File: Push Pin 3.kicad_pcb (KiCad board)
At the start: 2 copper layers, 95 x 77.4 mm, 27 parts, among them J1 Screw_Terminal_01x02, J10 Screw_Terminal_01x02, J11 Screw_Terminal_01x02, J12 Screw_Terminal_01x02, J13 Screw_Terminal_01x02, J4 Screw_Terminal_01x02, J5 Screw_Terminal_01x02, J6 Screw_Terminal_01x02, J7 Screw_Terminal_01x02, J8 Screw_Terminal_01x02, J9 Screw_Terminal_01x02, SW1 SW_DPDT_x2, SW2 SW_DPDT_x2, SW3 SW_DPDT_x2, U1 LM2596S-ADJ

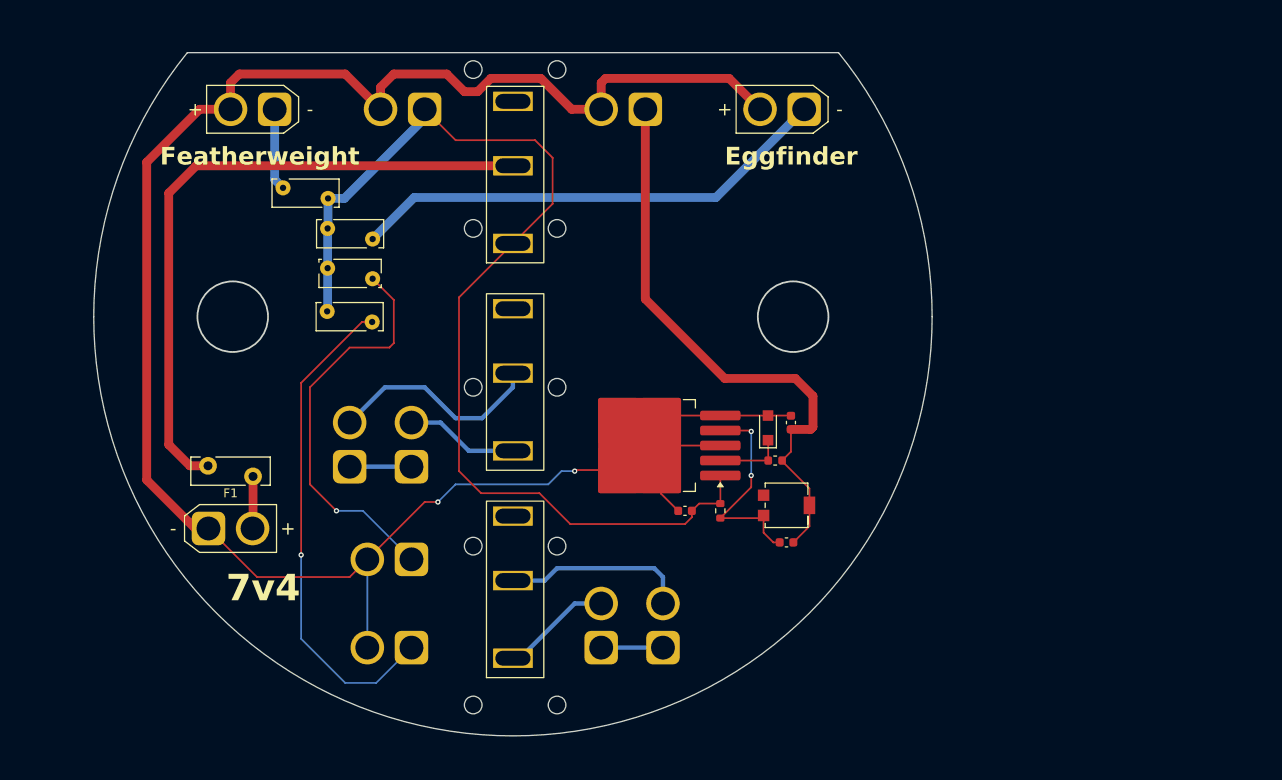
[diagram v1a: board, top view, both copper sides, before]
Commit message: Modif circuits
Ajout des circuits de protection de polarité inverse
Commentaires capacités de découplage
Jumper pour joindre batteries
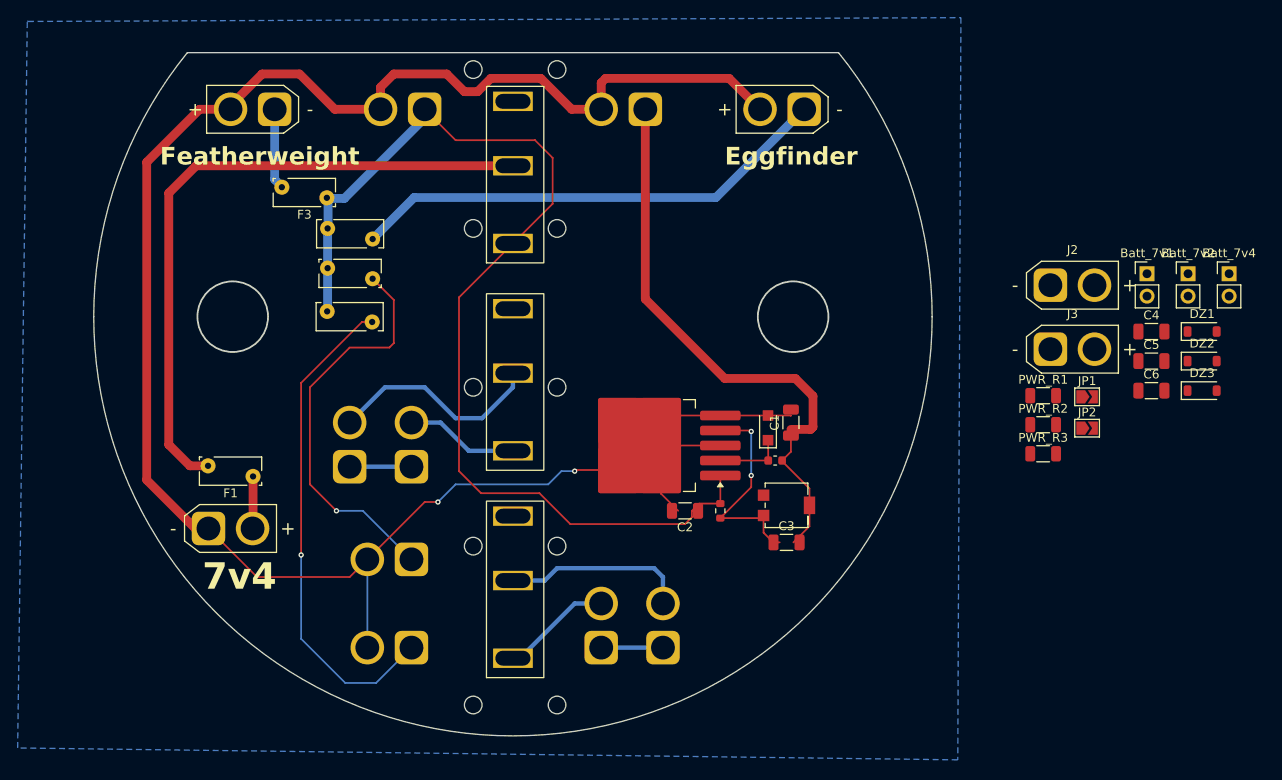
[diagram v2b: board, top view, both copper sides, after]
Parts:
- added Batt_7v1: Batt2_9V, Connector_PinHeader_2.54mm:PinHeader_1x02_P2.54mm_Vertical, F.Cu at (221.8, 95.1)
- added Batt_7v2: Batt1_9V, Connector_PinHeader_2.54mm:PinHeader_1x02_P2.54mm_Vertical, F.Cu at (226.5, 95.1)
- added Batt_7v4: Conn_01x02, Connector_PinHeader_2.54mm:PinHeader_1x02_P2.54mm_Vertical, F.Cu at (231.1, 95.1)
- added C4: 1uF, Capacitor_SMD:C_1206_3216Metric, F.Cu at (222.3, 101.7)
- added C5: 1uF, Capacitor_SMD:C_1206_3216Metric, F.Cu at (222.3, 105.0)
- added C6: 1uF, Capacitor_SMD:C_1206_3216Metric, F.Cu at (222.3, 108.4)
- added DZ1: SZMMSZ4679T1G, Diode_SMD:D_SOD-123, F.Cu at (228.1, 101.7)
- added DZ2: SZMMSZ4679T1G, Diode_SMD:D_SOD-123, F.Cu at (228.1, 105.0)
- added DZ3: SZMMSZ4679T1G, Diode_SMD:D_SOD-123, F.Cu at (228.1, 108.4)
- added J2: Screw_Terminal_01x02, Connector_AMASS:AMASS_XT30U-M_1x02_P5.0mm_Vertical, F.Cu at (210.9, 96.4)
- added J3: Screw_Terminal_01x02, Connector_AMASS:AMASS_XT30U-M_1x02_P5.0mm_Vertical, F.Cu at (210.9, 103.7)
- added JP1: SolderJumper_2_Open, Jumper:SolderJumper-2_P1.3mm_Open_TrianglePad1.0x1.5mm, F.Cu at (215.1, 109.1)
- added JP2: SolderJumper_2_Open, Jumper:SolderJumper-2_P1.3mm_Open_TrianglePad1.0x1.5mm, F.Cu at (215.1, 112.6)
- added PWR_R1: 100k, Resistor_SMD:R_1206_3216Metric, F.Cu at (210.1, 109.0)
- added PWR_R2: 100k, Resistor_SMD:R_1206_3216Metric, F.Cu at (210.1, 112.2)
- added PWR_R3: 100k, Resistor_SMD:R_1206_3216Metric, F.Cu at (210.1, 115.5)
- C1: value 220uF -> 1uF; footprint Capacitor_SMD:C_0603_1608Metric -> Capacitor_SMD:C_1206_3216Metric
- C2: value 150uF -> 1uF; footprint Capacitor_SMD:C_0603_1608Metric -> Capacitor_SMD:C_1206_3216Metric
- C3: value 30pF -> 1uF; footprint Capacitor_SMD:C_0603_1608Metric -> Capacitor_SMD:C_1206_3216Metric
- F1: footprint Fuse:Fuse_Bourns_MF-RHT300 -> Fuse:Fuse_Bourns_MF-RHT070
- F3: footprint Fuse:Fuse_Bourns_MF-RHT050 -> Fuse:Fuse_Bourns_MF-RHT070
- moved F3 0.15 mm to (128.9, 86.5)
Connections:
- C1 pad 1: Net-(J12-Pin_1) -> Net-(J5-Pin_2)
- C1 pad 2: V- -> GND
- C2 pad 1: V+ -> 7v4
- C2 pad 2: V- -> GND
- C3 pad 1: Net-(U1-FB) -> 7v4
- C3 pad 2: Net-(J12-Pin_1) -> GND
- F1 pad 1: Net-(J1-Pin_2) -> Net-(DZ1-K)
- F1 pad 2: Net-(SW3A-B) -> 7v4
- F2 pad 1: V+ -> 7v4
- F2 pad 2: Net-(J8-Pin_1) -> Net-(J1-Pin_2)
- F3 pad 1: V+ -> 7v4
- F3 pad 2: Net-(J13-Pin_1) -> Net-(J5-Pin_2)
- J1 pad 1: V- -> GND
- J4 pad 1: Net-(J4-Pin_1) -> GND
- J4 pad 2: Net-(J4-Pin_2) -> 7v4
- J5 pad 1: Net-(J4-Pin_1) -> GND
- J6 pad 1: Net-(J6-Pin_1) -> GND
- J6 pad 2: Net-(J6-Pin_2) -> 7v4
- J7 pad 1: Net-(J6-Pin_1) -> unconnected-(J7-Pin_1-Pad1)
- J7 pad 2: Net-(J7-Pin_2) -> unconnected-(J7-Pin_2-Pad2)
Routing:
- net Net-(J6-Pin_1): track 7.00 -> 0.00 mm
- net Net-(J4-Pin_1): track 7.00 -> 0.00 mm
- net GND: track 0.00 -> 7.00 mm
- net (no net): track 0.00 -> 7.00 mm
- net V-: track 225.3 -> 223.8 mm
- net Net-(J8-Pin_1): vias 1 -> 0
- net Net-(J1-Pin_2): vias 0 -> 1
- added copper zone on B.Cu, net GND

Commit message: PCB au complet
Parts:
- removed D2: D_Schottky, Diode_SMD:Nexperia_CFP3_SOD-123W
- removed F4, F5: Fuse, Fuse:Fuse_Bourns_MF-RHT050
- removed J10, J11, J12, J13, J8, J9: Screw_Terminal_01x02, Connector_AMASS:AMASS_XT30U-M_1x02_P5.0mm_Vertical
- removed L1: 47uH, Inductor_SMD:L_0603_1608Metric
- removed R1: 1k, Resistor_SMD:R_0603_1608Metric
- removed R2: 2k, Potentiometer_SMD:Potentiometer_Bourns_3214G_Horizontal
- removed SW1, SW2, SW3: SW_DPDT_x2, Library:Omrun_SS-01GL13
- removed U1: LM2596S-ADJ, Package_TO_SOT_SMD:TO-263-5_TabPin3
- added Q1: NTR4101PT1G, NTR4101PT1G:SOT-23-3_1P4X3P040_ONS, F.Cu at (141.0, 90.5)
- added Q2: NTR4101PT1G, NTR4101PT1G:SOT-23-3_1P4X3P040_ONS, B.Cu at (165.0, 126.0)
- added Q3: NTR4101PT1G, NTR4101PT1G:SOT-23-3_1P4X3P040_ONS, F.Cu at (136.0, 97.5)
- added SW4: SW_DPDT_x2, Library:Omrun_SS-01GL13, F.Cu at (150.0, 83.4)
- added SW5: SW_DPDT_x2, Library:Omrun_SS-01GL13, F.Cu at (150.0, 129.9)
- added SW6: SW_DPDT_x2, Library:Omrun_SS-01GL13, F.Cu at (150.0, 106.9)
- added U2: LDO_4v2-MIC5209-4.2YS-TR, footprints:SOT-223_S_MCH, F.Cu at (182.0, 86.2)
- Batt_7v1, Batt_7v2: footprint Connector_PinHeader_2.54mm:PinHeader_1x02_P2.54mm_Vertical -> Connector_AMASS:AMASS_XT30U-M_1x02_P5.0mm_Vertical; moved to B.Cu
- Batt_7v4: footprint Connector_PinHeader_2.54mm:PinHeader_1x02_P2.54mm_Vertical -> Connector_AMASS:AMASS_XT30U-M_1x02_P5.0mm_Vertical
- DZ2, J1, J2, J3, PWR_R2: moved to B.Cu
- J5: moved to F.Cu
- moved Batt_7v4 114.1 mm to (120.5, 123.0), turned to 180 degrees
- moved DZ3 96.3 mm to (132.5, 97.0), turned to 90 degrees
- moved DZ1 89.0 mm to (140.3, 87.0)
- moved Batt_7v2 87.5 mm to (140.0, 108.5), turned to 90 degrees
- moved JP1 87.5 mm to (128.2, 98.5), turned to 180 degrees
- moved PWR_R3 81.2 mm to (132.5, 91.5), turned to 90 degrees
- moved J6 79.3 mm to (117.5, 75.5), turned to 0 degrees
- moved J3 78.5 mm to (132.5, 108.5), turned to 90 degrees
- moved C3 75.3 mm to (120.0, 81.5), turned to 180 degrees
- moved PWR_R1 74.0 mm to (140.5, 84.0), turned to 180 degrees
- moved JP2 73.3 mm to (142.5, 122.8), turned to -90 degrees
- moved Batt_7v1 72.9 mm to (162.5, 137.5), turned to 90 degrees
- moved J7 67.2 mm to (183.5, 74.5), turned to 180 degrees
- moved DZ2 62.1 mm to (169.5, 125.5), turned to 90 degrees
- moved J2 58.3 mm to (169.5, 137.5), turned to 90 degrees
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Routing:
- net V-: track 223.8 -> 0.00 mm, vias 2 -> 0
- net V+: track 121.9 -> 0.00 mm
- net 9V: track 0.00 -> 74.4 mm, vias 0 -> 1
- net Net-(SW3A-B): track 74.2 -> 0.00 mm
- net Net-(Batt_7v4-Pin_2): track 0.00 -> 74.1 mm
- net Net-(J12-Pin_1): track 67.6 -> 0.00 mm
- net 9V_GND: track 0.00 -> 57.8 mm, vias 0 -> 1
- net Net-(J9-Pin_1): track 56.1 -> 0.00 mm, vias 1 -> 0
- net Net-(J10-Pin_1): track 55.0 -> 0.00 mm
- net Net-(J8-Pin_1): track 45.9 -> 0.00 mm
- net Net-(Batt_7v2-Pin_1): track 0.00 -> 45.2 mm, vias 0 -> 1
- net Net-(Q3-D): track 0.00 -> 44.3 mm
- net Net-(J4-Pin_2): track 25.8 -> 0.00 mm
- net Net-(U1-FB): track 24.6 -> 0.00 mm, vias 2 -> 0
- net GND: track 7.00 -> 31.5 mm, vias 0 -> 2
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- added copper zone on F.Cu, net 7v4
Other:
- board size 95 x 77.4 mm -> 92 x 75.9 mm
- board text added: "100k"
- board text added: "1uF"
- board text added: "9V"
- board text added: "Arming PCB V1"
- board text added: "Batterie 2S"
- board text added: "C NO NC"
- board text added: "Cameras"
- board text added: "Easymini"
- board text added: "EggFinder"
- board text added: "Juillet 2025 - Alexis G. - Nathan A. - Vincent T."
- board text added: "MIC5209"
- board text added: "NTR4101"
- board text added: "Solder to join 9V batteries"
- board text added: "Zener"
- board text removed: "7v4"
- board text removed: "Cam"
- board text removed: "EasyMini"
- board text removed: "Eggfinder"
- board text removed: "Featherweight"

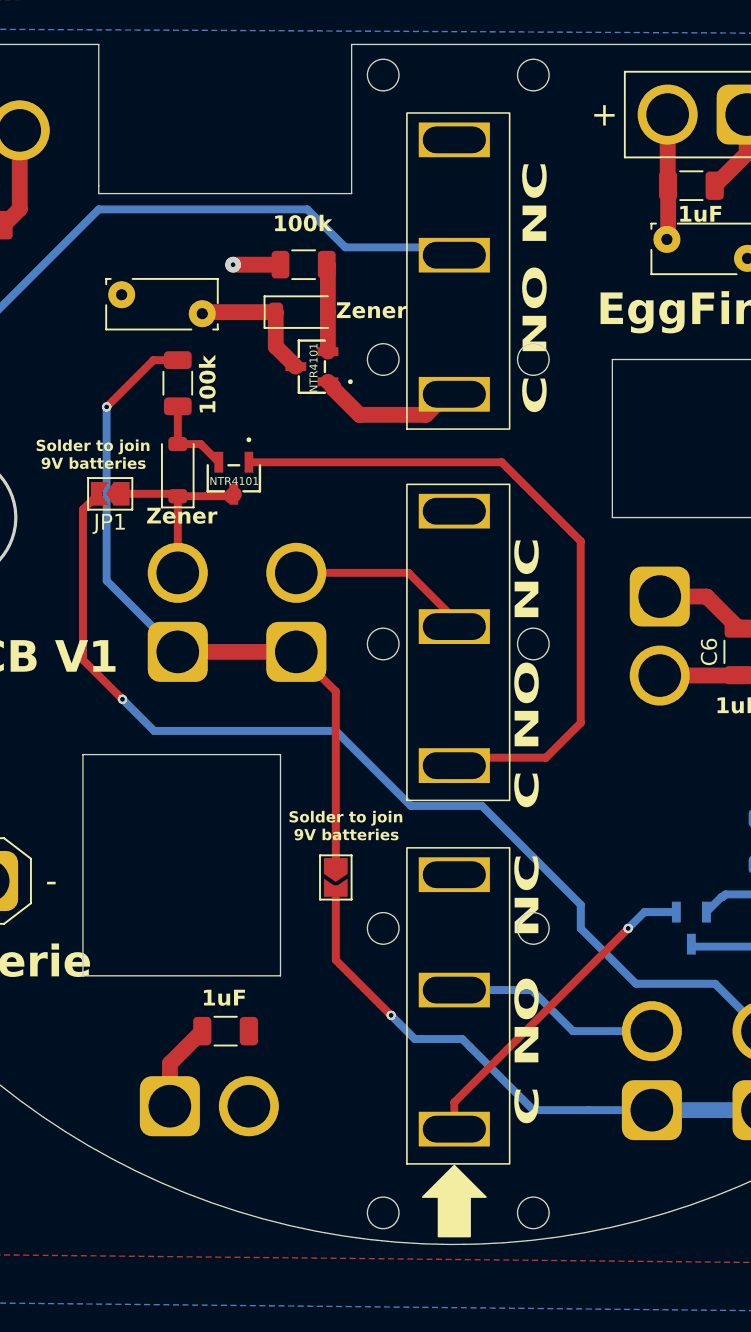
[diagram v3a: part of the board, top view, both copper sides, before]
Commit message: modif switch position
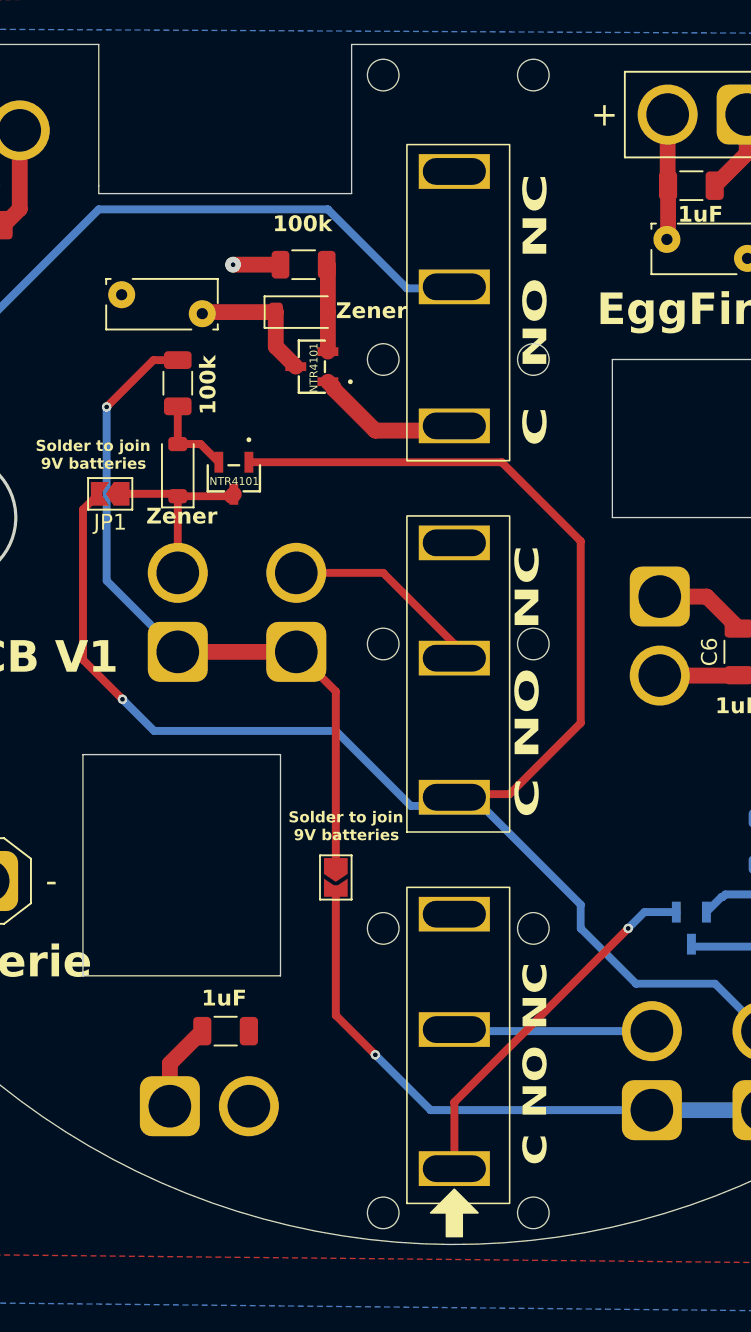
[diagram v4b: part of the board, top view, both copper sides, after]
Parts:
- moved SW5 2.50 mm to (150.0, 132.4)
- moved SW4 2.00 mm to (150.0, 85.4)
- moved SW6 2.00 mm to (150.0, 108.9)
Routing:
- net Net-(Q2-D): track 20.7 -> 23.2 mm
- net 9V_GND: track 57.8 -> 59.9 mm
- net Net-(Batt_7v2-Pin_2): track 11.2 -> 12.8 mm
- net Net-(Batt_7v4-Pin_2): track 74.1 -> 75.2 mm
- net Net-(Batt_7v1-Pin_2): track 13.6 -> 12.6 mm
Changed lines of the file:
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@@
 	(footprint "Library:Omrun_SS-01GL13"
 		(layer "F.Cu")
-		(at 150 129.9 90)
+		(at 150 132.4 90)
 		(property "Reference" "SW5"
 			(at 0 3.5 90)
@@
 	(footprint "Library:Omrun_SS-01GL13"
 		(layer "F.Cu")
-		(at 150 106.9 90)
+		(at 150 108.9 90)
 		(property "Reference" "SW6"
 			(at 0 3.5 90)
@@
 	(footprint "Library:Omrun_SS-01GL13"
 		(layer "F.Cu")
-		(at 150 83.4 90)
+		(at 150 85.4 90)
 		(property "Reference" "SW4"
 			(at 0 3.5 90)
@@
 	(gr_poly
 		(pts
-			(xy 149 145.5) (xy 149 143) (xy 148 143) (xy 150 141) (xy 152 143) (xy 151 143) (xy 151 145.5)
+			(xy 149.5 145.5) (xy 149.5 144) (xy 148.5 144) (xy 150 142.5) (xy 151.5 144) (xy 150.5 144) (xy 150.5 145.5)
 		)
 		(stroke
@@
 	(gr_poly
 		(pts
-			(xy 149 145.5) (xy 149 143) (xy 148 143) (xy 150 141) (xy 152 143) (xy 151 143) (xy 151 145.5)
+			(xy 149.5 145.5) (xy 149.5 144) (xy 148.5 144) (xy 150 142.5) (xy 151.5 144) (xy 150.5 144) (xy 150.5 145.5)
 		)
 		(stroke
@@
 	)
 	(gr_text "C NO  NC"
-		(at 155.5 118.5 90)
+		(at 155.5 119 90)
 		(layer "F.SilkS")
 		(effects
@@
 		)
 	)
-	(gr_text "C NO  NC"
-		(at 155.5 138.5 90)
+	(gr_text "C NO NC"
+		(at 156 141 90)
 		(layer "F.SilkS")
 		(effects
 			(font
-				(size 1.5 2.5)
+				(size 1.5 2)
 				(thickness 0.375)
 				(bold yes)
@@
 		)
 	)
-	(gr_text "C NO NC"
-		(at 156 93.5 90)
+	(gr_text "C  NO NC"
+		(at 156 95.5 90)
 		(layer "F.SilkS")
 		(effects
@@
 	)
 	(segment
-		(start 157.5 132.5)
-		(end 154.9 129.9)
+		(start 162.5 132.5)
+		(end 150.98995 132.5)
 		(width 0.5)
 		(layer "B.Cu")
@@
 	)
 	(segment
-		(start 154.9 129.9)
-		(end 150 129.9)
+		(start 150.78995 132.3)
+		(end 150 132.3)
 		(width 0.5)
 		(layer "B.Cu")
@@
 	)
 	(segment
-		(start 162.5 132.5)
-		(end 157.5 132.5)
+		(start 150.98995 132.5)
+		(end 150.78995 132.3)
 		(width 0.5)
 		(layer "B.Cu")
@@
 	)
 	(segment
-		(start 142.5 128)
-		(end 142.5 123.504903)
+		(start 145 134)
+		(end 142.5 131.5)
 		(width 0.5)
 		(layer "F.Cu")
@@
 	)
 	(segment
-		(start 146 131.5)
-		(end 142.5 128)
+		(start 142.5 131.5)
+		(end 142.5 123.504903)
 		(width 0.5)
 		(layer "F.Cu")
@@
 	)
 	(via
-		(at 146 131.5)
+		(at 145 134)
 		(size 0.6)
 		(drill 0.3)
@@
 	)
 	(segment
-		(start 151 133.5)
-		(end 150.5 133)
-		(width 0.5)
-		(layer "B.Cu")
-		(net 3)
-	)
-	(segment
-		(start 148 133)
-		(end 147.5 133)
-		(width 0.5)
-		(layer "B.Cu")
-		(net 3)
-	)
-	(segment
-		(start 162.5 137.5)
-		(end 158.5 137.5)
-		(width 0.5)
-		(layer "B.Cu")
-		(net 3)
-	)
-	(segment
-		(start 158.5 137.5)
-		(end 155 137.5)
-		(width 0.5)
-		(layer "B.Cu")
-		(net 3)
-	)
-	(segment
-		(start 150.5 133)
-		(end 148 133)
-		(width 0.5)
-		(layer "B.Cu")
-		(net 3)
-	)
-	(segment
-		(start 147.5 133)
-		(end 146 131.5)
+		(start 145 134)
+		(end 148.5 137.5)
 		(width 0.5)
 		(layer "B.Cu")
@@
 	)
 	(segment
-		(start 155 137.5)
-		(end 151 133.5)
-		(width 0.5)
-		(layer "B.Cu")
-		(net 3)
-	)
-	(segment
 		(start 162.5 137.5)
 		(end 169.5 137.5)
@@
 	)
 	(segment
+		(start 148.5 137.5)
+		(end 162.5 137.5)
+		(width 0.5)
+		(layer "B.Cu")
+		(net 3)
+	)
+	(segment
 		(start 163.5 74.5)
 		(end 163.5 78.975)
@@
 	)
 	(segment
-		(start 147.1 103.5)
-		(end 150 106.4)
+		(start 150 108)
+		(end 150 108.9)
+		(width 0.5)
+		(layer "F.Cu")
+		(net 5)
+	)
+	(segment
+		(start 145.5 103.5)
+		(end 150 108)
 		(width 0.5)
 		(layer "F.Cu")
@@
 	(segment
 		(start 140 103.5)
-		(end 147.1 103.5)
+		(end 145.5 103.5)
 		(width 0.5)
 		(layer "F.Cu")
@@
 	)
 	(segment
-		(start 115.5 107.499999)
-		(end 111.75 103.75)
+		(start 149.9 85.5)
+		(end 150 85.4)
 		(width 0.5)
 		(layer "B.Cu")
@@
 	)
 	(segment
-		(start 115.5 123)
-		(end 115.5 107.499999)
+		(start 147 85.5)
+		(end 149.9 85.5)
 		(width 0.5)
 		(layer "B.Cu")
@@
 	)
 	(segment
-		(start 111.75 96.25)
-		(end 127.5 80.5)
+		(start 127.5 80.5)
+		(end 142 80.5)
 		(width 0.5)
 		(layer "B.Cu")
@@
 	)
 	(segment
-		(start 140.7 80.5)
-		(end 143.1 82.9)
+		(start 115.5 107.499999)
+		(end 111.75 103.75)
 		(width 0.5)
 		(layer "B.Cu")
@@
 	)
 	(segment
-		(start 127.5 80.5)
-		(end 140.7 80.5)
+		(start 115.5 123)
+		(end 115.5 107.499999)
 		(width 0.5)
 		(layer "B.Cu")
@@
 	)
 	(segment
-		(start 143.1 82.9)
-		(end 150 82.9)
+		(start 111.75 96.25)
+		(end 127.5 80.5)
 		(width 0.5)
 		(layer "B.Cu")
@@
 	)
 	(segment
+		(start 142 80.5)
+		(end 147 85.5)
+		(width 0.5)
+		(layer "B.Cu")
+		(net 8)
+	)
+	(segment
 		(start 185.95 80)
 		(end 185.95 81.3222)
@@
 	)
 	(segment
-		(start 144 93.5)
+		(start 145 94.5)
 		(end 142.354212 91.854212)
 		(width 1)
@@
 	)
 	(segment
-		(start 142.354212 91.854212)
-		(end 142.354212 91.759212)
+		(start 150 94.2)
+		(end 149.7 94.5)
 		(width 1)
 		(layer "F.Cu")
@@
 	)
 	(segment
-		(start 150 91.7)
-		(end 148.2 93.5)
+		(start 149.7 94.5)
+		(end 145 94.5)
 		(width 1)
 		(layer "F.Cu")
@@
 	)
 	(segment
-		(start 142.354212 91.759212)
-		(end 142 91.405)
+		(start 142.354212 91.854212)
+		(end 142.354212 91.759212)
 		(width 1)
 		(layer "F.Cu")
@@
 	)
 	(segment
-		(start 148.2 93.5)
-		(end 144 93.5)
+		(start 142.354212 91.759212)
+		(end 142 91.405)
 		(width 1)
 		(layer "F.Cu")
@@
 	(segment
 		(start 150 137)
-		(end 150 138.7)
+		(end 150 141.2)
 		(width 0.5)
 		(layer "F.Cu")
@@
 	)
 	(segment
-		(start 158 113)
-		(end 155.8 115.2)
+		(start 158 101.5)
+		(end 158 113)
 		(width 0.5)
 		(layer "F.Cu")
@@
 	)
 	(segment
-		(start 153 96.5)
-		(end 158 101.5)
+		(start 153.5 117.5)
+		(end 150.2 117.5)
 		(width 0.5)
 		(layer "F.Cu")
@@
 	)
 	(segment
-		(start 155.8 115.2)
-		(end 150 115.2)
+		(start 150.2 117.5)
+		(end 150 117.7)
 		(width 0.5)
 		(layer "F.Cu")
@@
 	)
 	(segment
-		(start 137 96.5)
-		(end 153 96.5)
+		(start 158 113)
+		(end 153.5 117.5)
 		(width 0.5)
 		(layer "F.Cu")
@@
 	)
 	(segment
-		(start 158 101.5)
-		(end 158 113)
+		(start 137 96.5)
+		(end 153 96.5)
 		(width 0.5)
 		(layer "F.Cu")
@@
 	)
 	(segment
-		(start 149.2 115.2)
-		(end 150 115.2)
+		(start 153 96.5)
+		(end 158 101.5)
 		(width 0.5)
-		(layer "B.Cu")
+		(layer "F.Cu")
 		(net 23)
 	)
